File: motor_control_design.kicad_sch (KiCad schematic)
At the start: 96 parts, among them J1 TYPE-C-31-M-12, J10 5V, J2 SWD, J3 VBAT, J4 GND, J5 FC_M/P, J6 Conn_01x06, J7 Conn_01x04_Pin, J8 Conn_01x06, J9 GND, Q1 RF1S9540SM, Q10 2N7002, Q11 2N7002, Q12 2N7002, Q13 2N7002, Q14 RF1S9540SM, Q15 IRLZ44NS, Q16 2N7002, Q2 RF1S9540SM, Q3 IRLZ44NS, Q4 2N7002, Q5 2N7002, Q6 RF1S9540SM, Q7 IRLZ44NS, Q8 2N7002, Q9 IRLZ44NS, U1 STM32F401CCU6, U2 LT1962-3.3, U3 LTC4365DDB, U4 TPS563200, U5 SSM6N7002KFU_LF, Y1 16MHz

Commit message: nothing
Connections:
- net GND: no longer U3.1 (GND), U3.9 (GND)
- net at U5.2 (GATE1), U5.5 (GATE2): no longer U3.5 (GATE)
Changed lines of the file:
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@@
 	)
 	(junction
-		(at 165.1 148.59)
-		(diameter 0)
-		(color 0 0 0 0)
-	)
-	(junction
 		(at 207.01 96.52)
 		(diameter 0)
@@
 	)
 	(junction
-		(at 165.1 128.27)
-		(diameter 0)
-		(color 0 0 0 0)
-	)
-	(junction
 		(at 88.9 153.67)
 		(diameter 0)
@@
 	)
 	(junction
-		(at 167.64 148.59)
-		(diameter 0)
-		(color 0 0 0 0)
-	)
-	(junction
 		(at 132.08 160.02)
 		(diameter 0)
@@
 	(wire
 		(pts
-			(xy 191.77 128.27) (xy 165.1 128.27)
-		)
-		(stroke
-			(width 0)
-			(type default)
-		)
-	)
-	(wire
-		(pts
 			(xy 255.27 26.67) (xy 254 26.67)
 		)
@@
 	(wire
 		(pts
-			(xy 165.1 148.59) (xy 167.64 148.59)
-		)
-		(stroke
-			(width 0)
-			(type default)
-		)
-	)
-	(wire
-		(pts
 			(xy 100.33 80.01) (xy 106.68 80.01)
 		)
@@
 	(wire
 		(pts
-			(xy 165.1 128.27) (xy 137.16 128.27)
+			(xy 137.16 128.27) (xy 191.77 128.27)
 		)
 		(stroke
@@
 	(wire
 		(pts
-			(xy 157.48 148.59) (xy 165.1 148.59)
+			(xy 157.48 148.59) (xy 173.99 148.59)
 		)
 		(stroke
@@
 	(wire
 		(pts
-			(xy 173.99 148.59) (xy 167.64 148.59)
-		)
-		(stroke
-			(width 0)
-			(type default)
-		)
-	)
-	(wire
-		(pts
 			(xy 60.96 69.85) (xy 67.31 69.85)
 		)
@@
 		(on_board yes)
 		(dnp no)
+		(fields_autoplaced yes)
 		(property "Reference" "U3"
 			(at 166.878 126.746 0)

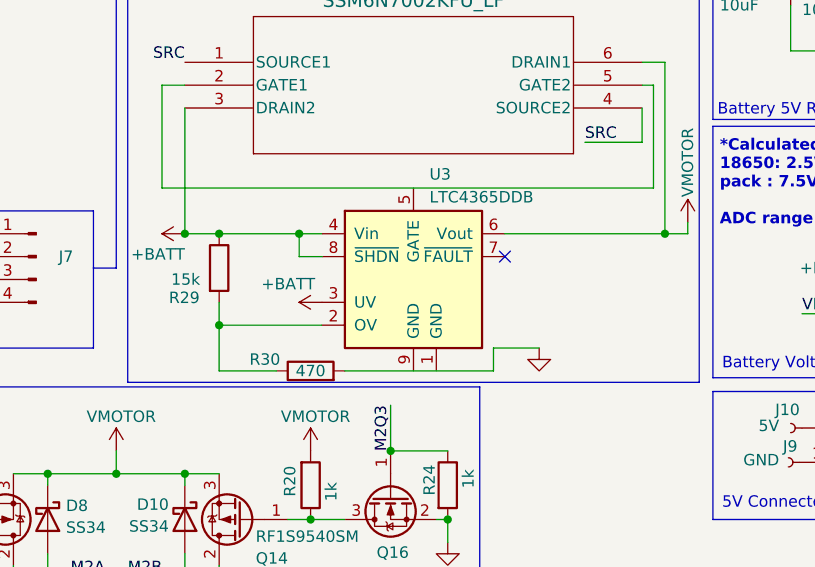
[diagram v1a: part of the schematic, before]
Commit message: small changes
fixed some ground plane connections, messed with the usbc footprint
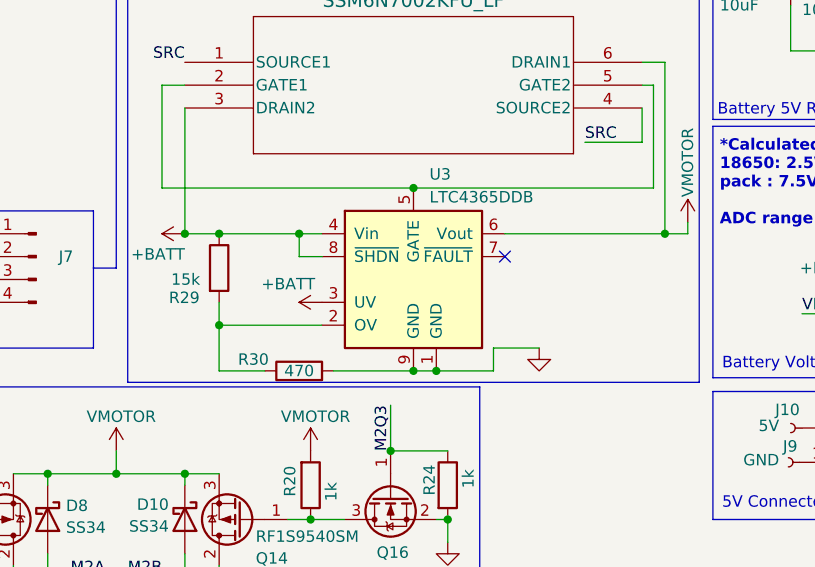
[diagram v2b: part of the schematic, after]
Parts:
- J1: footprint Connector_USB:USB_C_Receptacle_HRO_TYPE-C-31-M-12 -> CustomARES:USB_C_Receptacle_HRO_TYPE-C-31-M-12--MODIFIED
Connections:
- net GND: now also U3.1 (GND), U3.9 (GND)
- net at U3.5 (GATE): now also U5.2 (GATE1), U5.5 (GATE2)
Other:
- moved on the sheet: R30
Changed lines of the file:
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@@
 	)
 	(junction
+		(at 167.64 148.59)
+		(diameter 0)
+		(color 0 0 0 0)
+	)
+	(junction
 		(at 102.87 157.48)
 		(diameter 0)
@@
 	)
 	(junction
+		(at 165.1 148.59)
+		(diameter 0)
+		(color 0 0 0 0)
+	)
+	(junction
 		(at 105.918 21.59)
 		(diameter 0)
@@
 	)
 	(junction
+		(at 165.1 128.27)
+		(diameter 0)
+		(color 0 0 0 0)
+	)
+	(junction
 		(at 85.09 123.19)
 		(diameter 0)
@@
 	(wire
 		(pts
+			(xy 165.1 148.59) (xy 167.64 148.59)
+		)
+		(stroke
+			(width 0)
+			(type default)
+		)
+	)
+	(wire
+		(pts
 			(xy 265.43 140.97) (xy 270.51 140.97)
 		)
@@
 		)
 	)
+	(wire
+		(pts
+			(xy 167.64 148.59) (xy 173.99 148.59)
+		)
+		(stroke
+			(width 0)
+			(type default)
+		)
+	)
 	(polyline
 		(pts
@@
 	(wire
 		(pts
-			(xy 137.16 128.27) (xy 191.77 128.27)
+			(xy 137.16 128.27) (xy 165.1 128.27)
 		)
 		(stroke
@@
 	(wire
 		(pts
-			(xy 143.51 148.59) (xy 149.86 148.59)
+			(xy 143.51 148.59) (xy 148.59 148.59)
 		)
 		(stroke
@@
 	(wire
 		(pts
+			(xy 165.1 128.27) (xy 191.77 128.27)
+		)
+		(stroke
+			(width 0)
+			(type default)
+		)
+	)
+	(wire
+		(pts
 			(xy 152.4 133.35) (xy 152.4 135.89)
 		)
@@
 	(wire
 		(pts
-			(xy 157.48 148.59) (xy 173.99 148.59)
+			(xy 156.21 148.59) (xy 165.1 148.59)
 		)
 		(stroke
@@
 			)
 		)
-		(property "Footprint" "Connector_USB:USB_C_Receptacle_HRO_TYPE-C-31-M-12"
+		(property "Footprint" "CustomARES:USB_C_Receptacle_HRO_TYPE-C-31-M-12--MODIFIED"
 			(at 224.79 43.18 0)
 			(effects
@@
 	(symbol
 		(lib_id "Device:R")
-		(at 153.67 148.59 90)
+		(at 152.4 148.59 90)
 		(unit 1)
 		(exclude_from_sim no)
@@
 		(dnp no)
 		(property "Reference" "R30"
-			(at 148.59 147.32 90)
+			(at 147.32 147.32 90)
 			(effects
 				(font
@@
 		)
 		(property "Value" "470"
-			(at 153.67 148.59 90)
+			(at 152.4 148.59 90)
 			(effects
 				(font
@@
 		)
 		(property "Footprint" "Resistor_SMD:R_0603_1608Metric"
-			(at 153.67 150.368 90)
+			(at 152.4 150.368 90)
 			(effects
 				(font
@@
 		)
 		(property "Datasheet" "~"
-			(at 153.67 148.59 0)
+			(at 152.4 148.59 0)
 			(effects
 				(font
@@
 		)
 		(property "Description" "Resistor"
-			(at 153.67 148.59 0)
+			(at 152.4 148.59 0)
 			(effects
 				(font

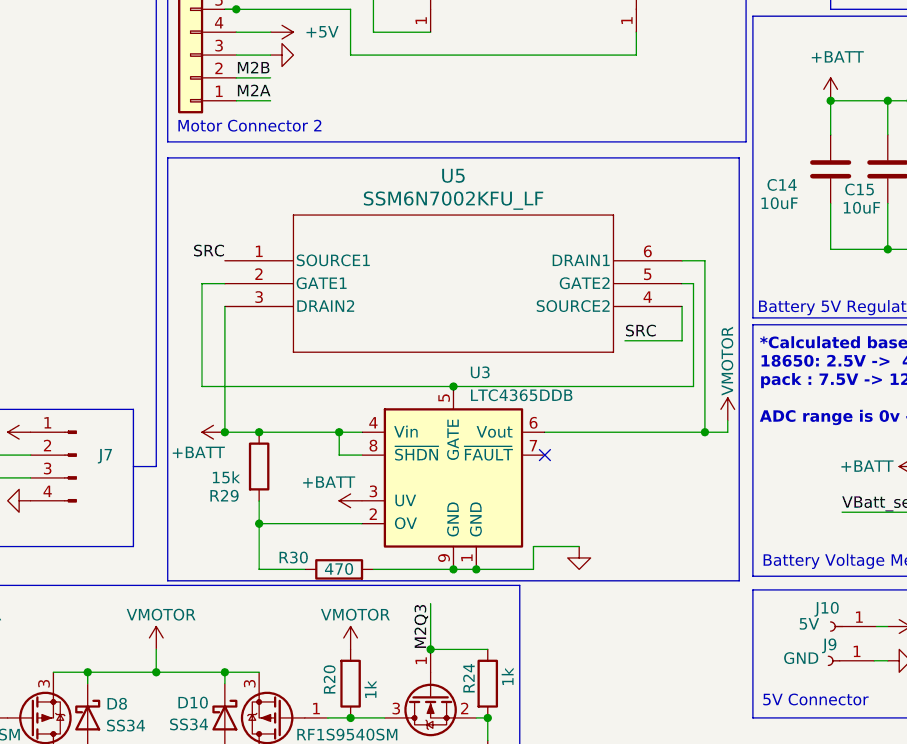
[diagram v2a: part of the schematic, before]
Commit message: IRF layout 80%
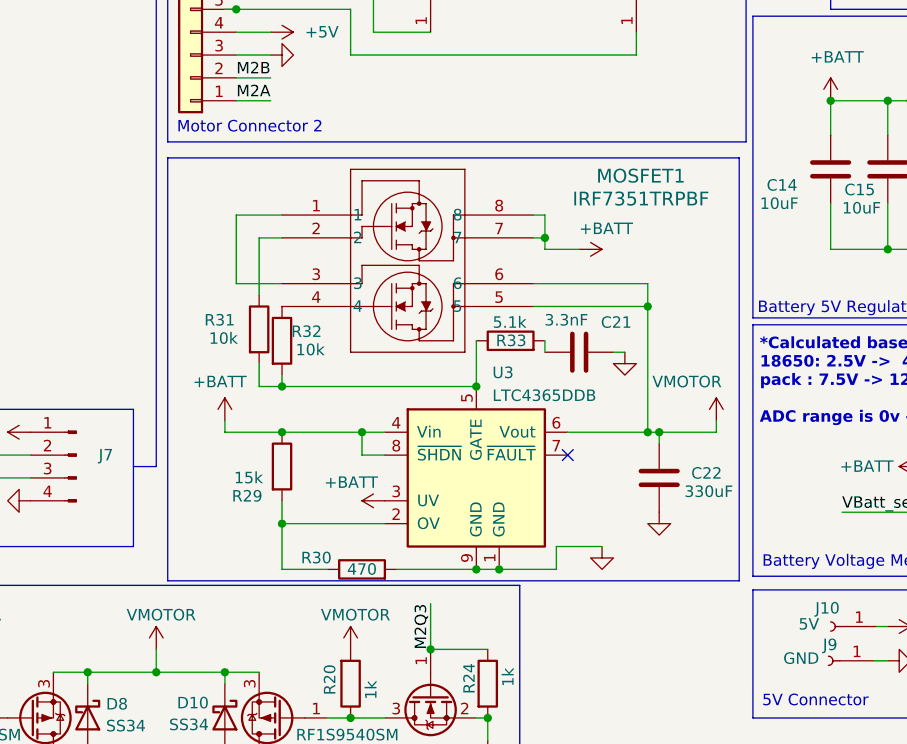
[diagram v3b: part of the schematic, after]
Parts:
- removed U5: SSM6N7002KFU_LF, CustomARES:SOT-363 US6_TOS-M, symbol Custom:SSM6N7002KFU_LF
- added C21: 3.3nF, Capacitor_SMD:C_0402_1005Metric, symbol Device:C
- added C22: 330uF, Capacitor_SMD:C_0402_1005Metric, symbol Device:C
- added MOSFET1: IRF7351TRPBF, CustomARES:PG-DSO-8-902_INF, symbol Custom:IRF7351TRPBF
- added R31, R32: 10k, Resistor_SMD:R_0402_1005Metric, symbol Device:R
- added R33: 5.1k, Resistor_SMD:R_0402_1005Metric, symbol Device:R
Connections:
- net +BATT: now also MOSFET1.7, MOSFET1.8
- net GND: now also C21.2, C22.2
- net VMOTOR: now also C22.1, MOSFET1.5, MOSFET1.6
- net at U3.5 (GATE): now also R31.2, R32.2, R33.1
- new net: MOSFET1.4, R32.1
- new net: C21.1, R33.2
- new net: MOSFET1.2, R31.1
- new net: MOSFET1.1, MOSFET1.3
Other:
- moved on the sheet: R29, R30, U3

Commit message: placement in progress
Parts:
- removed J5: FC_M/P, Connector_FFC-FPC:Molex_200528-0080_1x08-1MP_P1.00mm_Horizontal, symbol Connector_Generic:Conn_01x08
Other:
- note removed: "FC Connector"

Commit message: placement 95% done
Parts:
- removed J10: 5V, TestPoint:TestPoint_THTPad_4.0x4.0mm_Drill2.0mm, symbol Connector:Conn_01x01_Female
- removed J9: GND, TestPoint:TestPoint_THTPad_4.0x4.0mm_Drill2.0mm, symbol Connector:Conn_01x01_Female
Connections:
- net +BATT: now also C14.2; no longer C14.1
- net GND: now also C14.1; no longer C14.2
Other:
- note removed: "5V Connector"
- moved on the sheet: C14

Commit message: routing progress
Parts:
- removed CR1: SMBJ15A, CustomARES:DO-214AASMB_J-BEND_LTF, symbol Custom:SMBJ15A
- added D11, D13, D14, D18, D19, D21, D22, D23: PESD3V3U1UL, Diode_SMD:D_SOD-882, symbol Diode:PESD3V3U1UL
- added D15, D16, D17, D20: PESD5V0L1UL, Diode_SMD:D_SOD-882, symbol Diode:PESD5V0L1UL
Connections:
- net +3.3V: now also D14.1 (K)
- net GND: now also D11.2 (A), D13.2 (A), D14.2 (A), D15.2 (A), D16.2 (A), D17.2 (A), D18.2 (A), D19.2 (A), D20.2 (A), D21.1 (K), D22.1 (K), D23.1 (K)
- net NRST: now also D23.2 (A)
- net SCL: now also D19.1 (K)
- net SDA: now also D18.1 (K)
- net SWCLK: now also D21.2 (A)
- net SWDIO: now also D22.2 (A)
- net USB_D+: now also D13.1 (K)
- net USB_D-: now also D11.1 (K)
- net at J8.6 (Pin_6), Q11.1 (G): now also D15.1 (K)
- net at J6.6 (Pin_6), Q10.1 (G): now also D17.1 (K)
- net at J6.5 (Pin_5), Q8.1 (G): now also D20.1 (K)
- net at J8.5 (Pin_5), Q12.1 (G): now also D16.1 (K)
- no-connect marks 14 -> 16
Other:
- note removed: "* Verify MOSFET configuration and test w/ actual encoder"
- note removed: "TVS Diode"
- moved on the sheet: J2

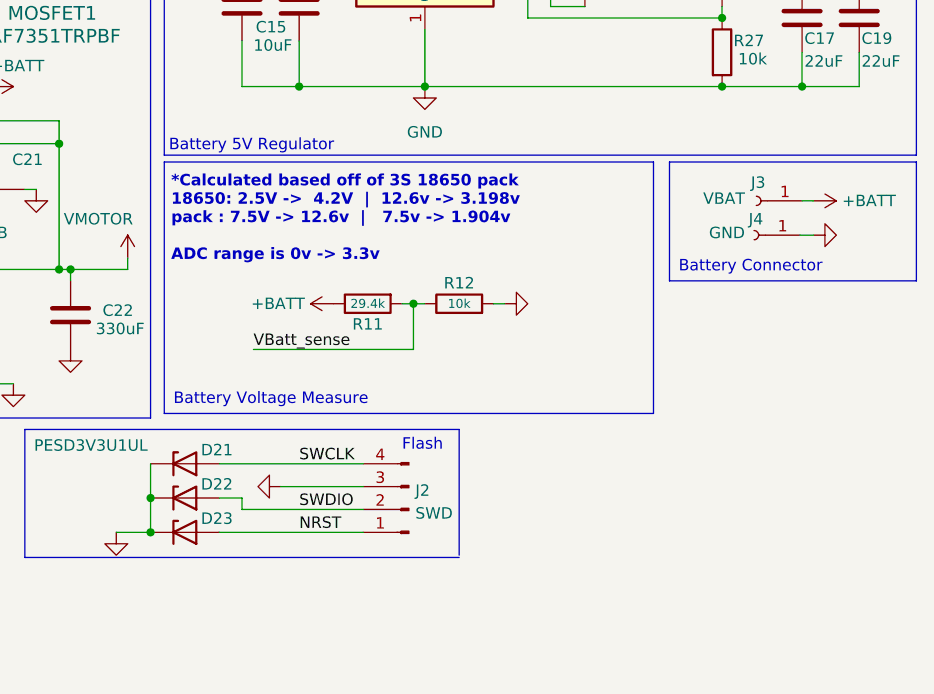
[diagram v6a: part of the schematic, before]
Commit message: xt30, cleaned up board
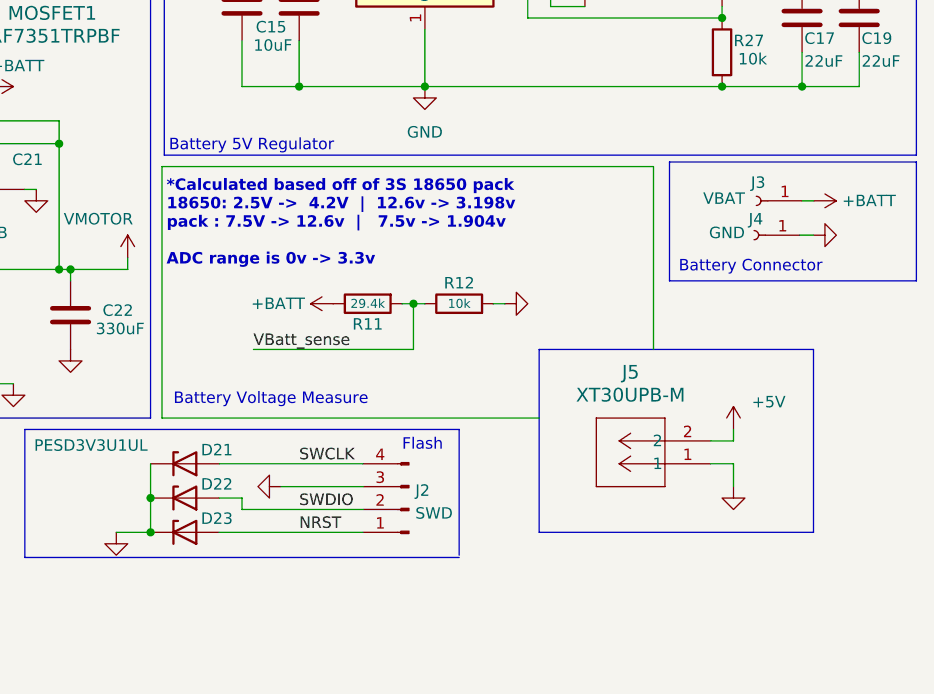
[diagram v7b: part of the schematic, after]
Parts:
- added J5: XT30UPB-M, CONN_XT30UPB-M_AMA, symbol Custom:XT30UPB-M
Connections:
- net +5V: now also J5.2
- net GND: now also J5.1

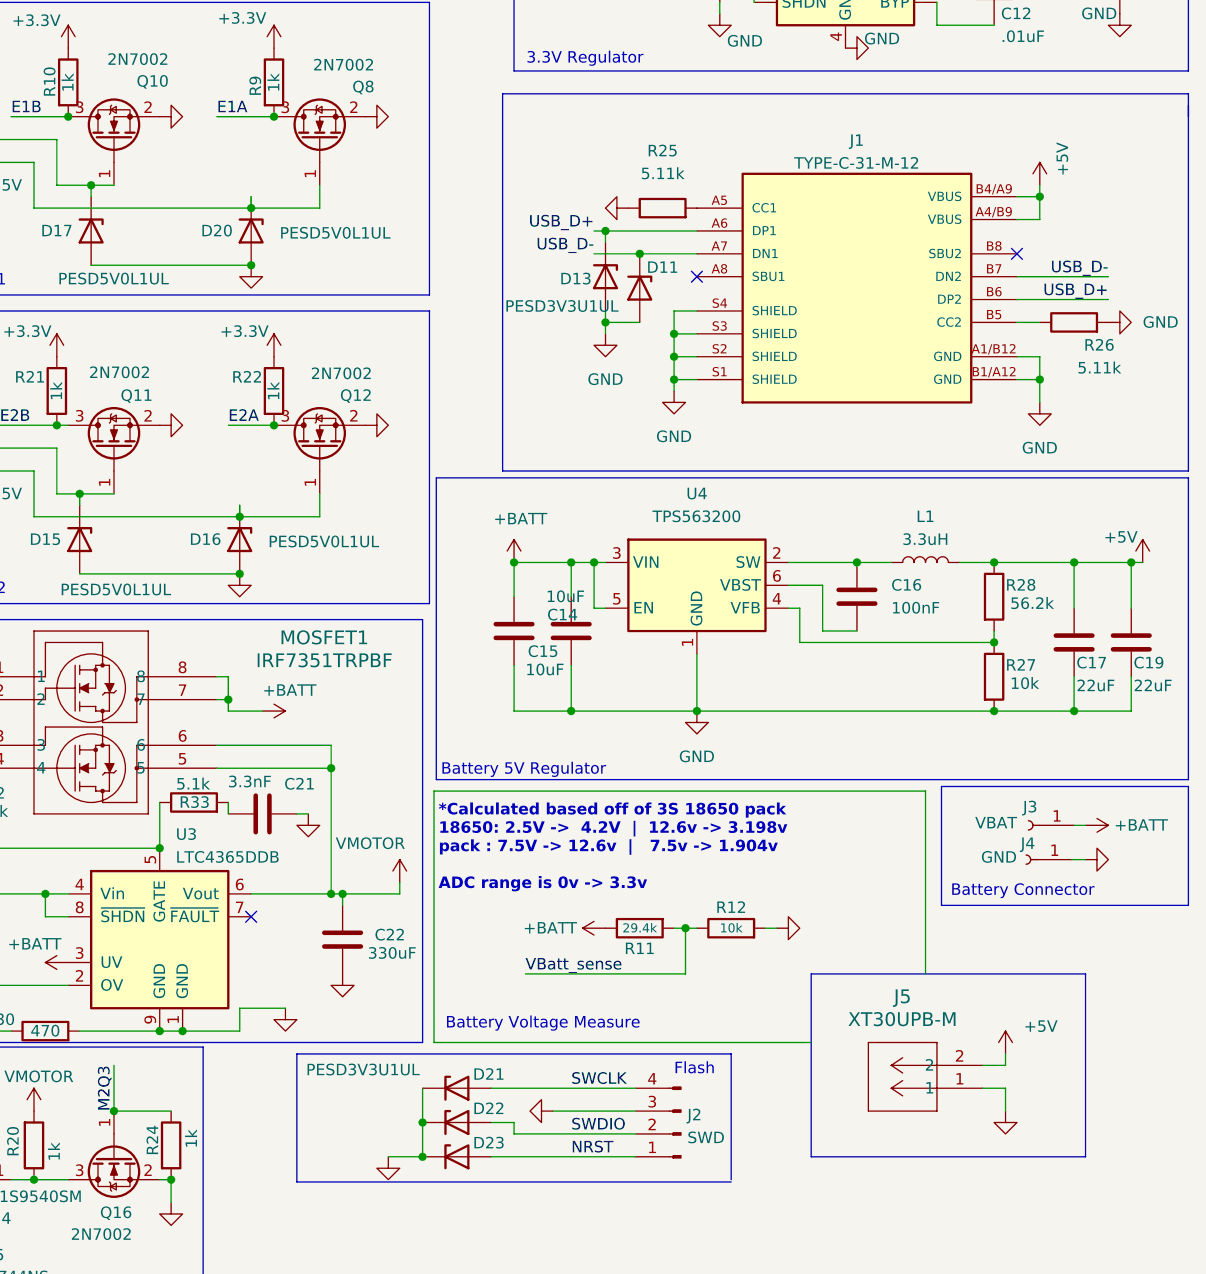
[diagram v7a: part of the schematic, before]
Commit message: connector change, files prepared
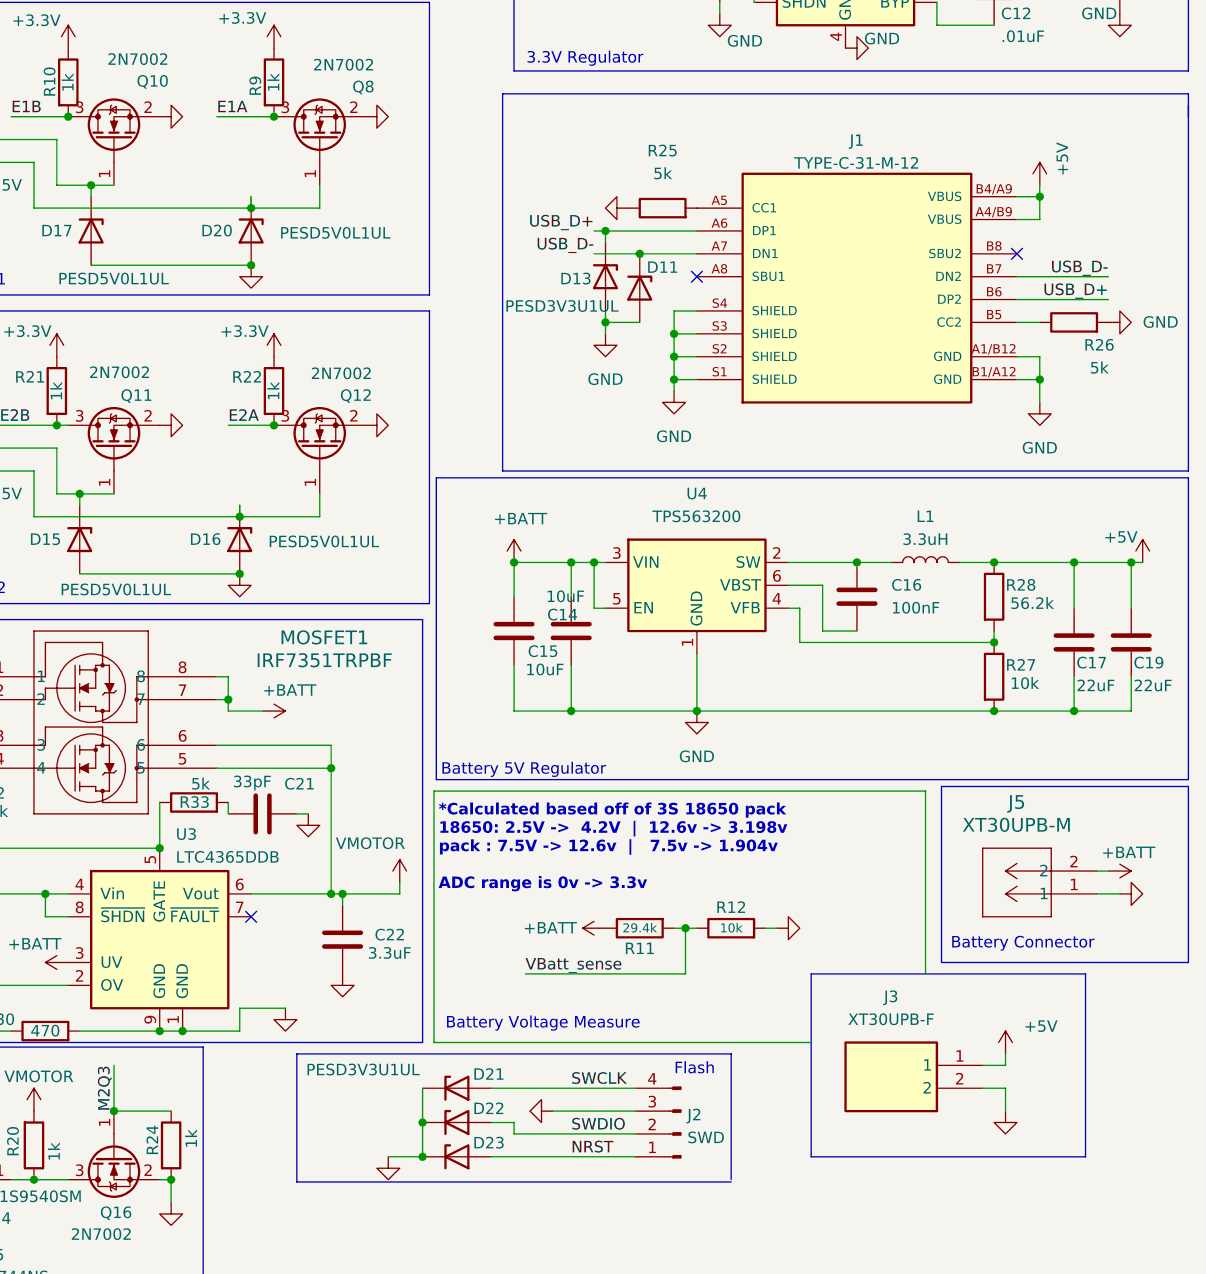
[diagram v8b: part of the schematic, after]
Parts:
- removed J3: VBAT, TestPoint:TestPoint_THTPad_4.0x4.0mm_Drill2.0mm, symbol Connector:Conn_01x01_Female
- removed J4: GND, TestPoint:TestPoint_THTPad_4.0x4.0mm_Drill2.0mm, symbol Connector:Conn_01x01_Female
- added J3: XT30UPB-F, CustomARES:XT30UPBF, symbol Custom:XT30UPB-F
- C12: LCSC Part (none) -> C15195
- C13, C14, C15: LCSC Part (none) -> C315248
- C16, C20: LCSC Part (none) -> C1525
- C17, C19: LCSC Part (none) -> C3845593
- C18: LCSC Part (none) -> C14445
- C21: value 3.3nF -> 33pF; LCSC Part (none) -> C70465
- C22: value 330uF -> 3.3uF; footprint Capacitor_SMD:C_0402_1005Metric -> Capacitor_SMD:C_0603_1608Metric; LCSC Part (none) -> C51412
- D11, D13, D14, D18, D19, D21, D22, D23: LCSC Part (none) -> C19829543
- D15, D16, D17, D20: LCSC Part (none) -> C3001948
- J2: LCSC Part (none) -> C160390
- J5: footprint CONN_XT30UPB-M_AMA -> CustomARES:CONN_XT30UPB-M_AMA; LCSC Part (none) -> C428721
- J6, J8: LCSC Part (none) -> C191914
- L1: LCSC Part (none) -> C7153195
- MOSFET1: LCSC Part (none) -> C68403
- R25, R26: value 5.11k -> 5k; LCSC Part (none) -> C166638
- R27, R31, R32: LCSC Part (none) -> C25531
- R28: LCSC Part (none) -> C54968
- R29: LCSC Part (none) -> C25539
- R30: LCSC Part (none) -> C25117
- R33: value 5.1k -> 5k; LCSC Part (none) -> C166638
- U2: LCSC Part (none) -> C107774
- U3: LCSC Part (none) -> C688318
- U4: LCSC Part (none) -> C97253
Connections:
- net +5V: now also J3.1; no longer J5.2
- net +BATT: now also J5.2
- net GND: now also J3.2
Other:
- moved on the sheet: J5
